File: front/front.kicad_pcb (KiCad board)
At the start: 2 copper layers, 182.2 x 132.1 mm, 4 parts, among them U1 LSM6DSO32TR, U2 VL53L8CXV0GC/1, U3 TCA9548APWR, U4 PCA9615DP

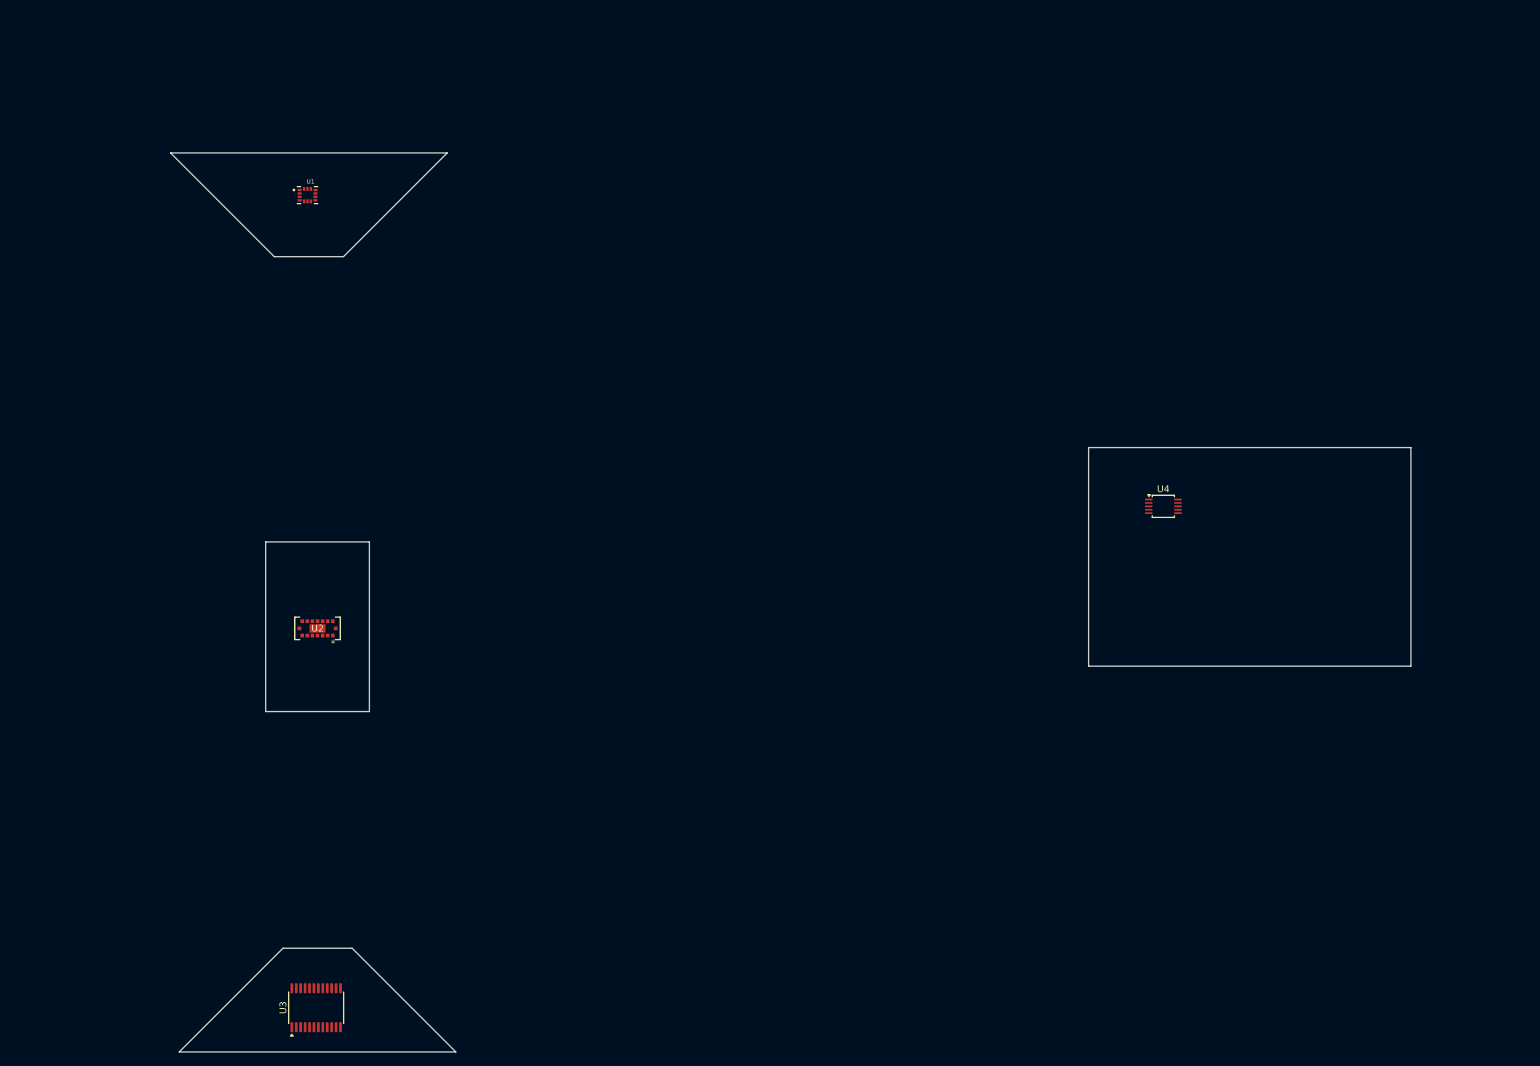
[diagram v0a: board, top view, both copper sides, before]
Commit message: script panelizes
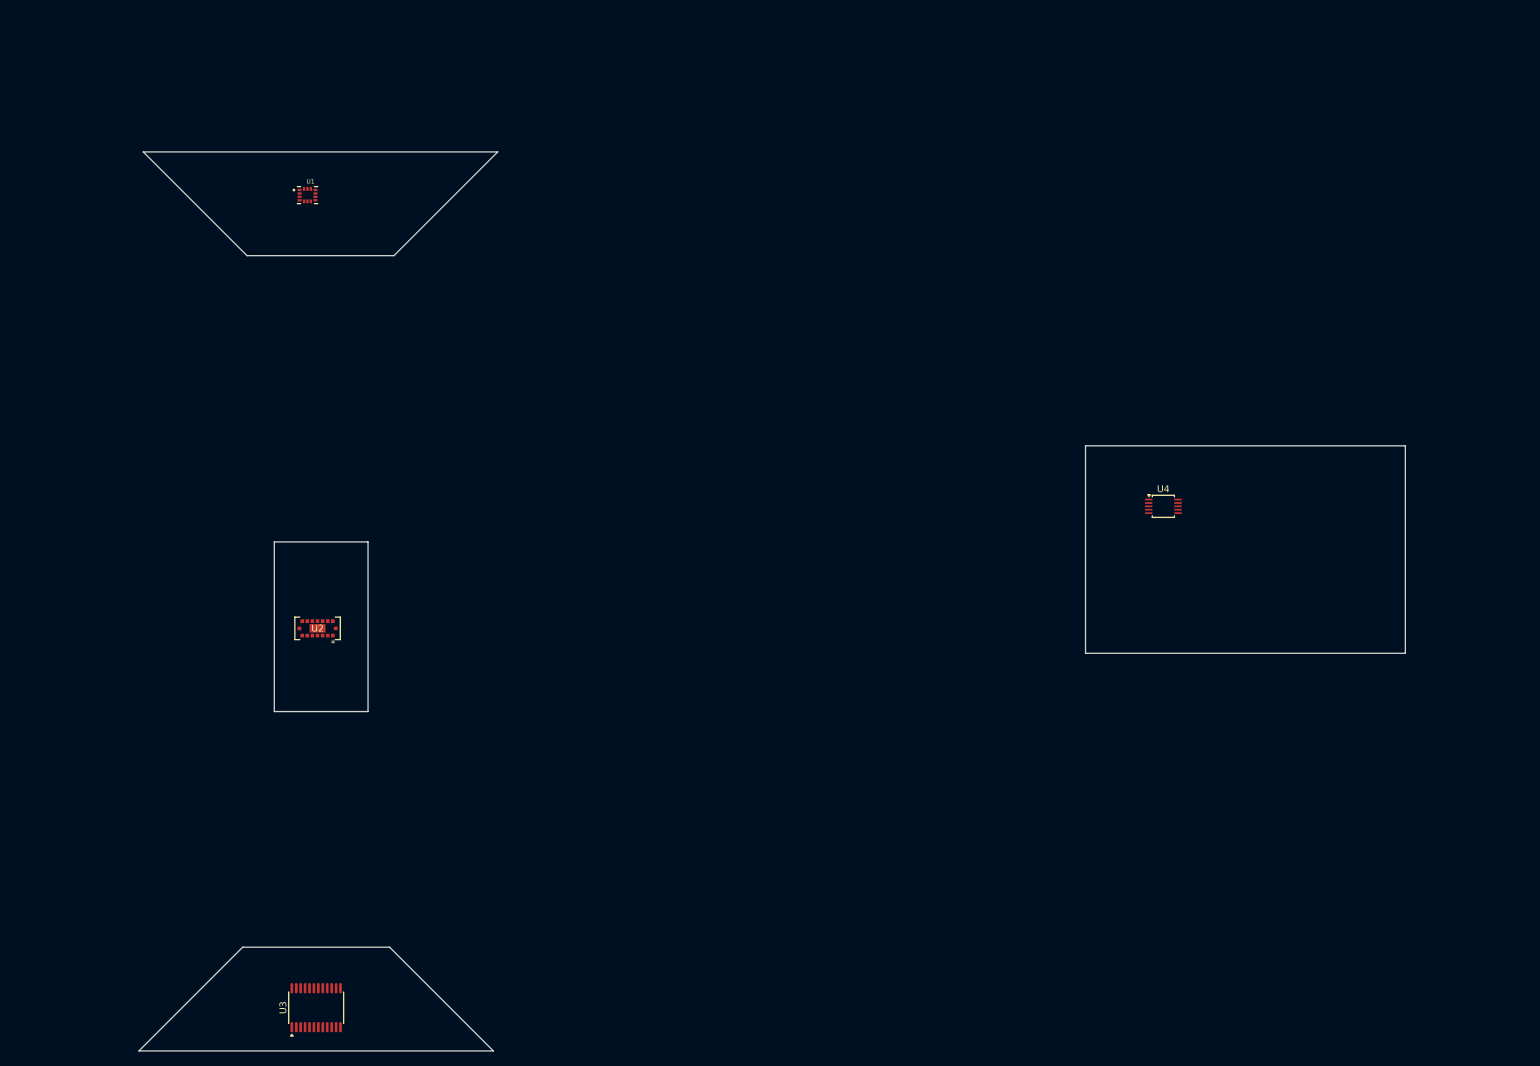
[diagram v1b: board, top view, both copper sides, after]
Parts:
- added REF**: Tab, PCM_kikit:Tab, F.Cu at (189.1, 106.6)
- added REF**: Tab, PCM_kikit:Tab, F.Cu at (78.7, 52.0)
- added REF**: Tab, PCM_kikit:Tab, F.Cu at (91.4, 168.9)
- added REF**: Tab, PCM_kikit:Tab, F.Cu at (77.4, 151.1)
- added REF**: Tab, PCM_kikit:Tab, F.Cu at (91.4, 34.2)
- added REF**: Tab, PCM_kikit:Tab, F.Cu at (69.8, 115.5)
- added REF**: Tab, PCM_kikit:Tab, F.Cu at (238.7, 82.5)
- added REF**: Tab, PCM_kikit:Tab, F.Cu at (86.4, 115.5)
- added REF**: Tab, PCM_kikit:Tab, F.Cu at (189.1, 82.5)
- added REF**: Tab, PCM_kikit:Tab, F.Cu at (69.8, 95.2)
- added REF**: Tab, PCM_kikit:Tab, F.Cu at (64.7, 34.2)
- added REF**: Tab, PCM_kikit:Tab, F.Cu at (238.7, 106.6)
- added REF**: Tab, PCM_kikit:Tab, F.Cu at (64.8, 168.9)
- added REF**: Tab, PCM_kikit:Tab, F.Cu at (86.4, 95.2)
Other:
- board size 182.2 x 132.1 mm -> 186.1 x 132.1 mm

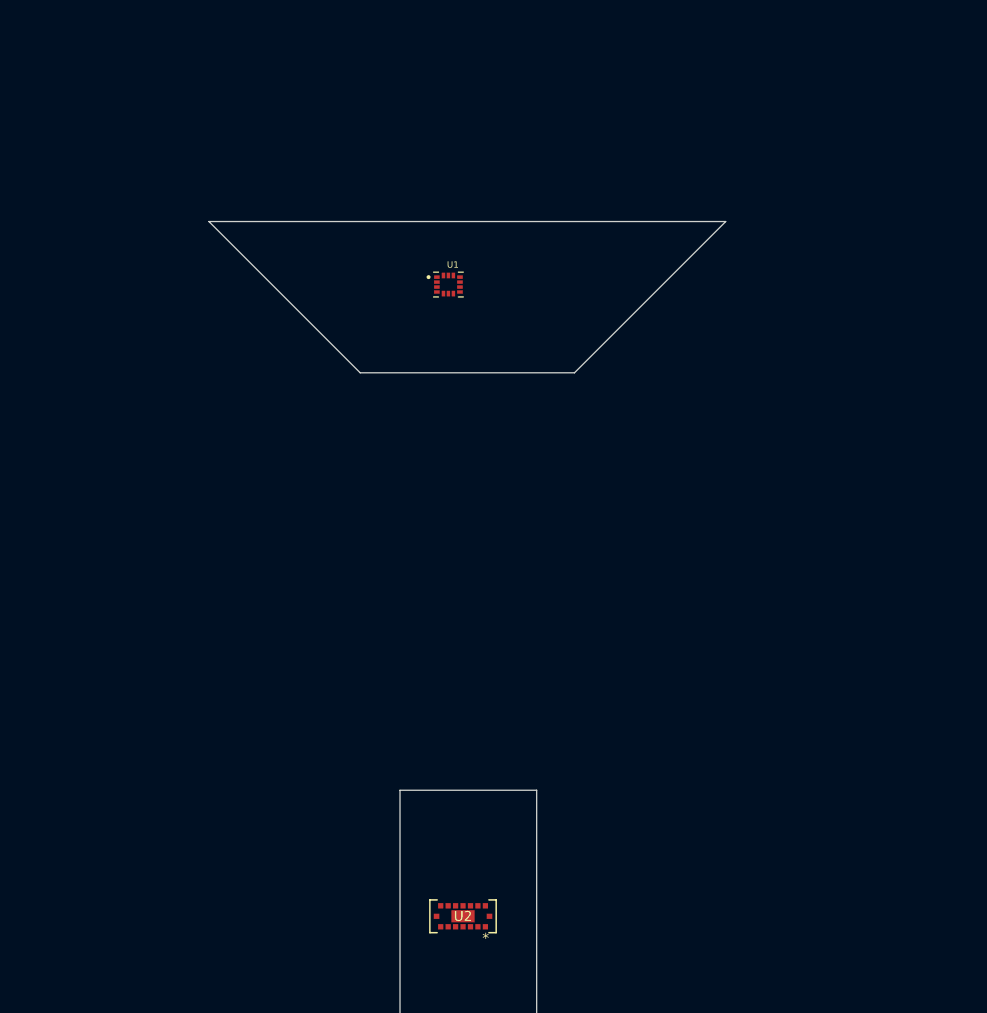
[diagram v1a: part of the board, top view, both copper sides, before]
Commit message: add some traces
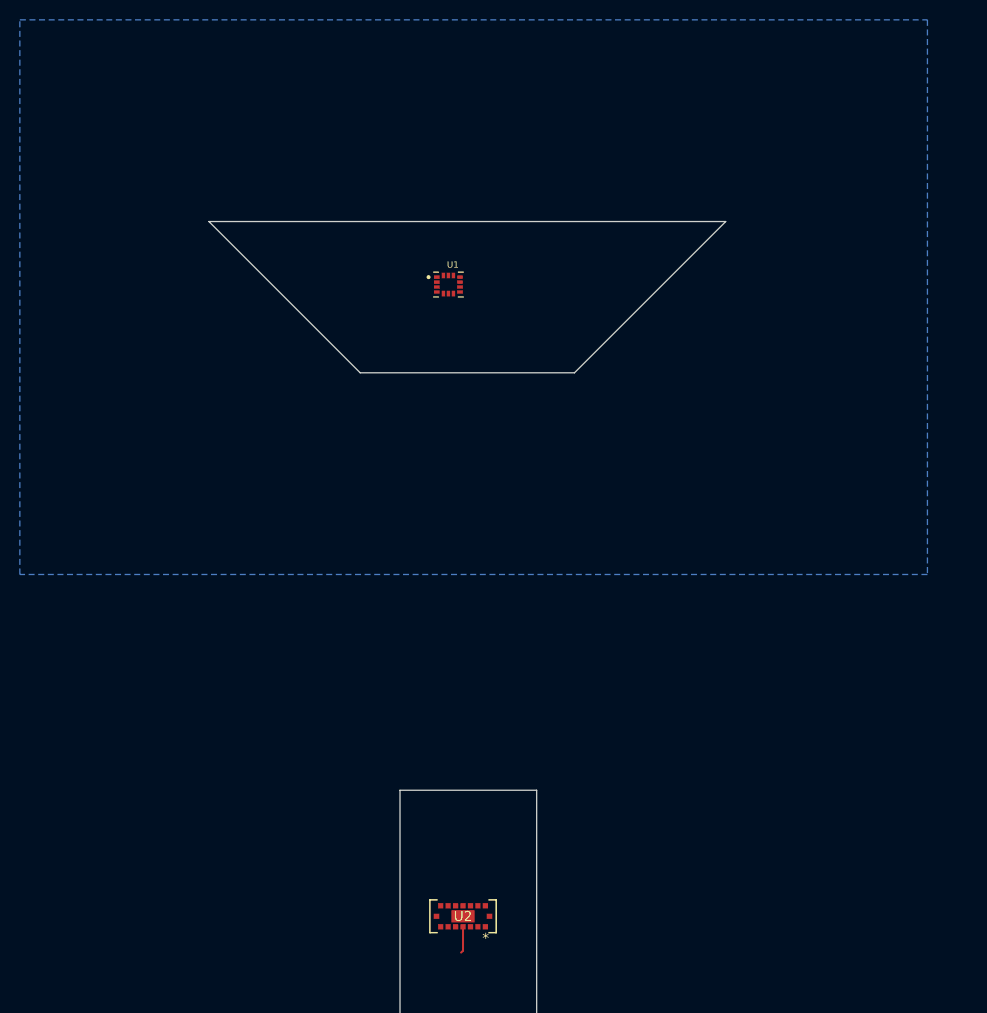
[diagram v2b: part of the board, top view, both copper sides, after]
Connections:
- U1 pad 6: unconnected-(U1-GND-Pad6) -> GND
- U1 pad 7: unconnected-(U1-GND__1-Pad7) -> GND
- U2 pad B4: unconnected-(U2-THERMALPAD-PadB4) -> GND
- U3 pad 12: unconnected-(U3-GND-Pad12) -> GND
- U4 pad 5: unconnected-(U4-V_{SS}-Pad5) -> GND
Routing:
- net unconnected-(U2-SDA/MOSI-PadA4): track 0.00 -> 2.69 mm
- added copper zone on B.Cu, net GND

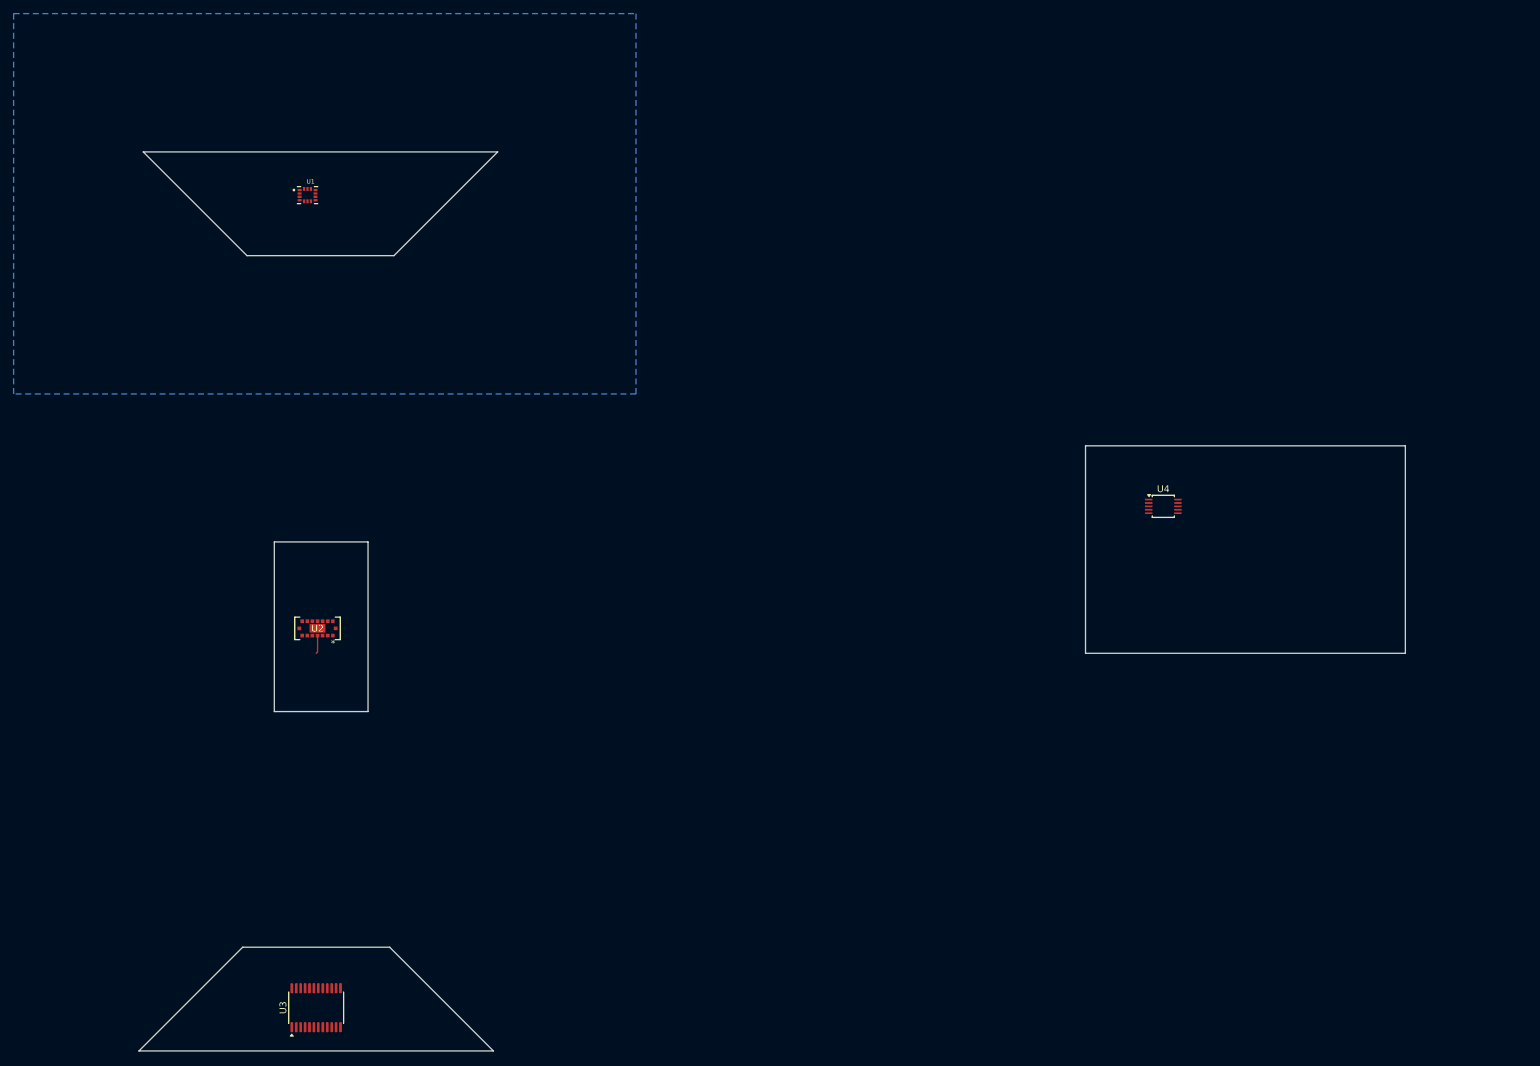
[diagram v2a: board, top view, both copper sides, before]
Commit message: undo panelizing
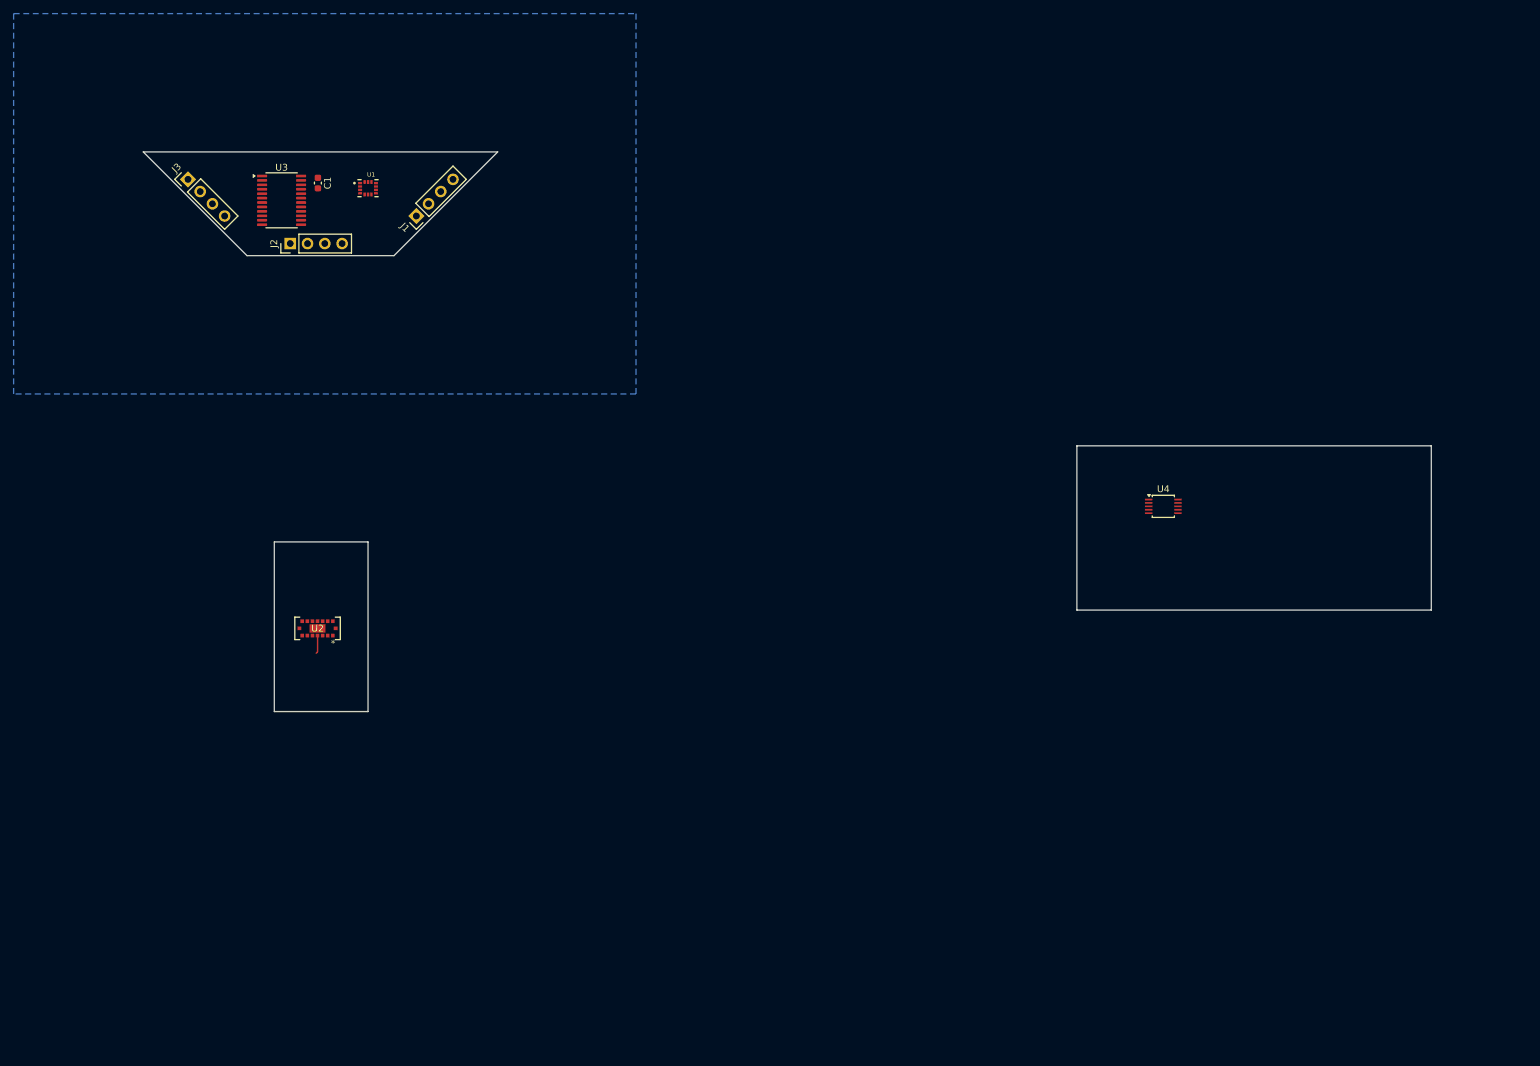
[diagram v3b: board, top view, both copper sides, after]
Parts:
- removed REF** (x14): Tab, PCM_kikit:Tab
- added C1: 1uF, Capacitor_SMD:C_0603_1608Metric, F.Cu at (77.7, 40.1)
- added J1: Conn_01x04, Connector_PinHeader_2.54mm:PinHeader_1x04_P2.54mm_Vertical, F.Cu at (92.2, 45.0)
- added J2: Conn_01x04, Connector_PinHeader_2.54mm:PinHeader_1x04_P2.54mm_Vertical, F.Cu at (73.7, 49.0)
- added J3: Conn_01x04, Connector_PinHeader_2.54mm:PinHeader_1x04_P2.54mm_Vertical, F.Cu at (58.6, 39.6)
- moved U3 118.7 mm to (72.4, 42.7), turned to 0 degrees
- moved U1 8.95 mm to (85.1, 40.9)
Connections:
- U3 pad 24: unconnected-(U3-VCC-Pad24) -> Net-(U3-VCC)
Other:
- board size 186.1 x 132.1 mm -> 189.2 x 82.2 mm
